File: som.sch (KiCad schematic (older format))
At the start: 22 parts, among them M1 SC606T

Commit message: Added TP Interface. Connector must yet be added
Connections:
- net labels added: LDO10_2P8, TP0_I2C_SCL, TP0_I2C_SDA, TP0_INT, TP0_RST
- wire segments 68 -> 69
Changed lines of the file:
@@
 Text GLabel 2800 2550 0    50   Input ~ 0
 ANT_MAIN
+Text GLabel 5000 2650 2    50   Input ~ 0
+TP0_RST
+Text GLabel 5000 2750 2    50   Input ~ 0
+TP0_INT
+Text GLabel 7400 2350 0    50   Input ~ 0
+TP0_I2C_SCL
+Text GLabel 7400 2450 0    50   Input ~ 0
+TP0_I2C_SDA
+Text GLabel 2450 1850 0    50   Input ~ 0
+LDO10_2P8
+Wire Wire Line
+	2450 1850 2800 1850
 Wire Bus Line
 	1750 4650 1750 5350

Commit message: Added annotations. Move to loclib
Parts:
- C1, C10, C7: footprint antmicro-footprints:0402-cap -> sc606-baseboard-footprints:0402-cap; symbol antmicroCapacitors0402:C_10p_0402 -> sc606-baseboard:C_10p_0402
- C11, C2, C8: footprint antmicro-footprints:0402-cap -> sc606-baseboard-footprints:0402-cap; symbol antmicroCapacitors0402:C_33p_0402 -> sc606-baseboard:C_33p_0402
- C12, C13, C3, C9: footprint antmicro-footprints:0402-cap -> sc606-baseboard-footprints:0402-cap; symbol antmicroCapacitors0402:C_100n_0402 -> sc606-baseboard:C_100n_0402
- C14, C4: footprint antmicro-footprints:0402-cap -> sc606-baseboard-footprints:0402-cap; symbol antmicroCapacitors0402:C_4u7_0402 -> sc606-baseboard:C_4u7_0402
- C15: renamed from C?; footprint antmicro-footprints:0402-cap -> sc606-baseboard-footprints:0402-cap; symbol antmicroCapacitors0402:C_33p_0402 -> sc606-baseboard:C_33p_0402
- C16: renamed from C?; footprint antmicro-footprints:0402-cap -> sc606-baseboard-footprints:0402-cap; symbol antmicroCapacitors0402:C_10p_0402 -> sc606-baseboard:C_10p_0402
- C5, C6: footprint antmicro-footprints:1206-cap -> sc606-baseboard-footprints:1206-cap; symbol antmicroCapacitorsmisc:C_100u_1206 -> sc606-baseboard:C_100u_1206
- D1: footprint antmicro-footprints:SOD-964 -> sc606-baseboard-footprints:SOD-964; symbol antmicroTVSDiodes:PTVS5V0Z1USKPYL -> sc606-baseboard:PTVS5V0Z1USKPYL
- M1: footprint antmicro-footprints:QUECTEL_SC606T -> sc606-baseboard-footprints:QUECTEL_SC606T; symbol antmicroModules:SC606T -> sc606-baseboard:SC606T
- R1: footprint antmicro-footprints:0402-res -> sc606-baseboard-footprints:0402-res; symbol antmicroResistors0402:R_47k_0402 -> sc606-baseboard:R_47k_0402
- R2: footprint antmicro-footprints:0402-res -> sc606-baseboard-footprints:0402-res; symbol antmicroResistors0402:R_0R_0402 -> sc606-baseboard:R_0R_0402
- TP1, TP2: renamed from TP?; footprint antmicro-footprints:Testpoint_smd_0_75mm -> sc606-baseboard-footprints:Testpoint_smd_0_75mm; symbol antmicroTestPoints:TP_SMD_0_75MM -> sc606-baseboard:TP_SMD_0_75MM

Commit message: Block diagram update
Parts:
- C1, C10, C16, C7: footprint sc606-baseboard-footprints:0402-cap -> antmicro-footprints:0402-cap; symbol sc606-baseboard:C_10p_0402 -> antmicroCapacitors0402:C_10p_0402
- C11, C15, C2, C8: footprint sc606-baseboard-footprints:0402-cap -> antmicro-footprints:0402-cap; symbol sc606-baseboard:C_33p_0402 -> antmicroCapacitors0402:C_33p_0402
- C12, C13, C3, C9: footprint sc606-baseboard-footprints:0402-cap -> antmicro-footprints:0402-cap; symbol sc606-baseboard:C_100n_0402 -> antmicroCapacitors0402:C_100n_0402
- C14, C4: footprint sc606-baseboard-footprints:0402-cap -> antmicro-footprints:0402-cap; symbol sc606-baseboard:C_4u7_0402 -> antmicroCapacitors0402:C_4u7_0402
- C5, C6: footprint sc606-baseboard-footprints:1206-cap -> antmicro-footprints:1206-cap; symbol sc606-baseboard:C_100u_1206 -> antmicroCapacitorsmisc:C_100u_1206
- D1: footprint sc606-baseboard-footprints:SOD-964 -> antmicro-footprints:SOD-964; symbol sc606-baseboard:PTVS5V0Z1USKPYL -> antmicroTVSDiodes:PTVS5V0Z1USKPYL
- M1: footprint sc606-baseboard-footprints:QUECTEL_SC606T -> antmicro-footprints:QUECTEL_SC606T; symbol sc606-baseboard:SC606T -> antmicroModules:SC606T
- R1: footprint sc606-baseboard-footprints:0402-res -> antmicro-footprints:0402-res; symbol sc606-baseboard:R_47k_0402 -> antmicroResistors0402:R_47k_0402
- R2: footprint sc606-baseboard-footprints:0402-res -> antmicro-footprints:0402-res; symbol sc606-baseboard:R_0R_0402 -> antmicroResistors0402:R_0R_0402
- TP1, TP2: footprint sc606-baseboard-footprints:Testpoint_smd_0_75mm -> antmicro-footprints:Testpoint_smd_0_75mm; symbol sc606-baseboard:TP_SMD_0_75MM -> antmicroTestPoints:TP_SMD_0_75MM

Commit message: Added connectors to LCD displays
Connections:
- net labels added: LDO17_2P85
- wire segments 69 -> 70
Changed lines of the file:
@@
 Wire Wire Line
 	2450 1850 2800 1850
+Text GLabel 2450 1950 0    50   Input ~ 0
+LDO17_2P85
+Wire Wire Line
+	2450 1950 2800 1950
 Wire Bus Line
 	1750 4650 1750 5350

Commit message: Added keypads and no flag connections to unused pins
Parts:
- removed R2: R_0R_0402, antmicro-footprints:0402-res, symbol antmicroResistors0402:R_0R_0402
- C1, C10, C16, C7: footprint antmicro-footprints:0402-cap -> sc606-baseboard-footprints:0402-cap; symbol antmicroCapacitors0402:C_10p_0402 -> sc606-baseboard:C_10p_0402
- C11, C15, C2, C8: footprint antmicro-footprints:0402-cap -> sc606-baseboard-footprints:0402-cap; symbol antmicroCapacitors0402:C_33p_0402 -> sc606-baseboard:C_33p_0402
- C12, C13, C3, C9: footprint antmicro-footprints:0402-cap -> sc606-baseboard-footprints:0402-cap; symbol antmicroCapacitors0402:C_100n_0402 -> sc606-baseboard:C_100n_0402
- C14, C4: footprint antmicro-footprints:0402-cap -> sc606-baseboard-footprints:0402-cap; symbol antmicroCapacitors0402:C_4u7_0402 -> sc606-baseboard:C_4u7_0402
- C5, C6: footprint antmicro-footprints:1206-cap -> sc606-baseboard-footprints:1206-cap; symbol antmicroCapacitorsmisc:C_100u_1206 -> sc606-baseboard:C_100u_1206
- D1: footprint antmicro-footprints:SOD-964 -> sc606-baseboard-footprints:SOD-964; symbol antmicroTVSDiodes:PTVS5V0Z1USKPYL -> sc606-baseboard:PTVS5V0Z1USKPYL
- M1: footprint antmicro-footprints:QUECTEL_SC606T -> sc606-baseboard-footprints:QUECTEL_SC606T; symbol antmicroModules:SC606T -> sc606-baseboard:SC606T
- R1: footprint antmicro-footprints:0402-res -> sc606-baseboard-footprints:0402-res; symbol antmicroResistors0402:R_47k_0402 -> sc606-baseboard:R_47k_0402
- TP1, TP2: footprint antmicro-footprints:Testpoint_smd_0_75mm -> sc606-baseboard-footprints:Testpoint_smd_0_75mm; symbol antmicroTestPoints:TP_SMD_0_75MM -> sc606-baseboard:TP_SMD_0_75MM
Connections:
- net labels added: DSI0_CLK_N, DSI0_CLK_P, DSI0_LN0_N, DSI0_LN0_P, DSI0_LN1_N, DSI0_LN1_P, DSI0_LN2_N, DSI0_LN2_P, DSI0_LN3_N, DSI0_LN3_P, PWRKEY, USB_VBUS, VOL_DOWN, VOL_UP
- net labels removed: 5V0_SYS, TP0_INT, TP0_RST
- no-connect marks 44 -> 88

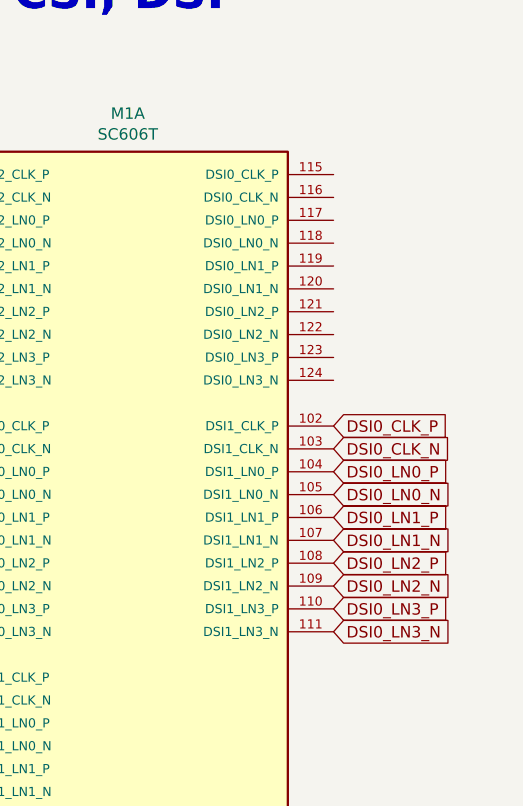
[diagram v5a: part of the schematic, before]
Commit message: LT9611 connected to all needed sources
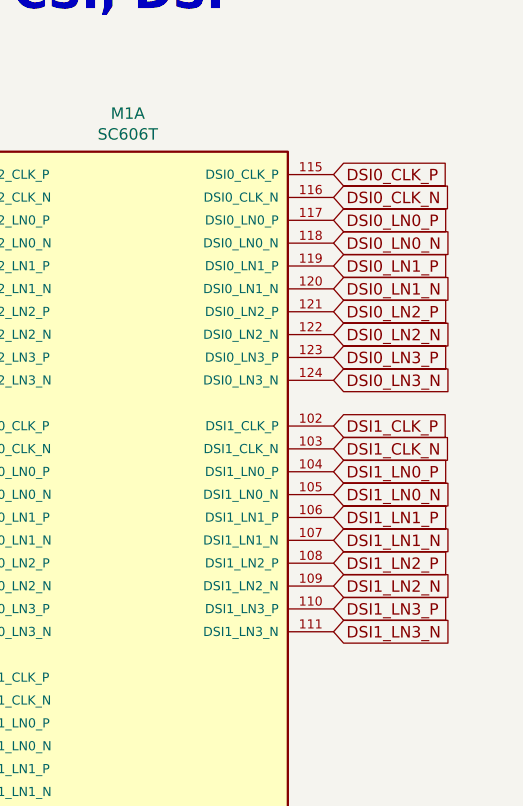
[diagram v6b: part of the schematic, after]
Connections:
- net DSI0_CLK_N: now also M1.116 (DSI0_CLK_N); no longer M1.103 (DSI1_CLK_N)
- net DSI0_CLK_P: now also M1.115 (DSI0_CLK_P); no longer M1.102 (DSI1_CLK_P)
- net DSI0_LN0_N: now also M1.118 (DSI0_LN0_N); no longer M1.105 (DSI1_LN0_N)
- net DSI0_LN0_P: now also M1.117 (DSI0_LN0_P); no longer M1.104 (DSI1_LN0_P)
- net DSI0_LN1_N: now also M1.120 (DSI0_LN1_N); no longer M1.107 (DSI1_LN1_N)
- net DSI0_LN1_P: now also M1.119 (DSI0_LN1_P); no longer M1.106 (DSI1_LN1_P)
- net DSI0_LN2_N: now also M1.122 (DSI0_LN2_N); no longer M1.109 (DSI1_LN2_N)
- net DSI0_LN2_P: now also M1.121 (DSI0_LN2_P); no longer M1.108 (DSI1_LN2_P)
- net DSI0_LN3_N: now also M1.124 (DSI0_LN3_N); no longer M1.111 (DSI1_LN3_N)
- net DSI0_LN3_P: now also M1.123 (DSI0_LN3_P); no longer M1.110 (DSI1_LN3_P)
- new net DSI1_CLK_N: M1.103 (DSI1_CLK_N)
- new net DSI1_CLK_P: M1.102 (DSI1_CLK_P)
- new net DSI1_LN0_N: M1.105 (DSI1_LN0_N)
- new net DSI1_LN0_P: M1.104 (DSI1_LN0_P)
- new net DSI1_LN1_N: M1.107 (DSI1_LN1_N)
- new net DSI1_LN1_P: M1.106 (DSI1_LN1_P)
- new net DSI1_LN2_N: M1.109 (DSI1_LN2_N)
- new net DSI1_LN2_P: M1.108 (DSI1_LN2_P)
- new net DSI1_LN3_N: M1.111 (DSI1_LN3_N)
- new net DSI1_LN3_P: M1.110 (DSI1_LN3_P)
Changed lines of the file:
@@
 NoConn ~ 5000 5850
 Text GLabel 14650 7700 2    50   Input ~ 0
+DSI1_LN3_N
+Text GLabel 14650 7600 2    50   Input ~ 0
+DSI1_LN3_P
+Text GLabel 14650 7500 2    50   Input ~ 0
+DSI1_LN2_N
+Text GLabel 14650 7400 2    50   Input ~ 0
+DSI1_LN2_P
+Text GLabel 14650 7300 2    50   Input ~ 0
+DSI1_LN1_N
+Text GLabel 14650 7200 2    50   Input ~ 0
+DSI1_LN1_P
+Text GLabel 14650 7100 2    50   Input ~ 0
+DSI1_LN0_N
+Text GLabel 14650 7000 2    50   Input ~ 0
+DSI1_LN0_P
+Text GLabel 14650 6900 2    50   Input ~ 0
+DSI1_CLK_N
+Text GLabel 14650 6800 2    50   Input ~ 0
+DSI1_CLK_P
+Text GLabel 14650 6600 2    50   Input ~ 0
 DSI0_LN3_N
-Text GLabel 14650 7600 2    50   Input ~ 0
+Text GLabel 14650 6500 2    50   Input ~ 0
 DSI0_LN3_P
-Text GLabel 14650 7500 2    50   Input ~ 0
+Text GLabel 14650 6400 2    50   Input ~ 0
 DSI0_LN2_N
-Text GLabel 14650 7400 2    50   Input ~ 0
+Text GLabel 14650 6300 2    50   Input ~ 0
 DSI0_LN2_P
-Text GLabel 14650 7300 2    50   Input ~ 0
+Text GLabel 14650 6200 2    50   Input ~ 0
 DSI0_LN1_N
-Text GLabel 14650 7200 2    50   Input ~ 0
+Text GLabel 14650 6100 2    50   Input ~ 0
 DSI0_LN1_P
-Text GLabel 14650 7100 2    50   Input ~ 0
+Text GLabel 14650 6000 2    50   Input ~ 0
 DSI0_LN0_N
-Text GLabel 14650 7000 2    50   Input ~ 0
-DSI0_LN0_P
-Text GLabel 14650 6900 2    50   Input ~ 0
-DSI0_CLK_N
-Text GLabel 14650 6800 2    50   Input ~ 0
-DSI0_CLK_P
 Wire Bus Line
 	1750 4650 1750 5350
@@
 Wire Bus Line
 	11650 7800 11650 8700
+Text GLabel 14650 5900 2    50   Input ~ 0
+DSI0_LN0_P
+Text GLabel 14650 5800 2    50   Input ~ 0
+DSI0_CLK_N
+Text GLabel 14650 5700 2    50   Input ~ 0
+DSI0_CLK_P
 $EndSCHEMATC
